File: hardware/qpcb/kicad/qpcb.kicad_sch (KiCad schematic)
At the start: 9 parts, among them J1 SWD Connector, J2 UART0 Connector, U1 Pico

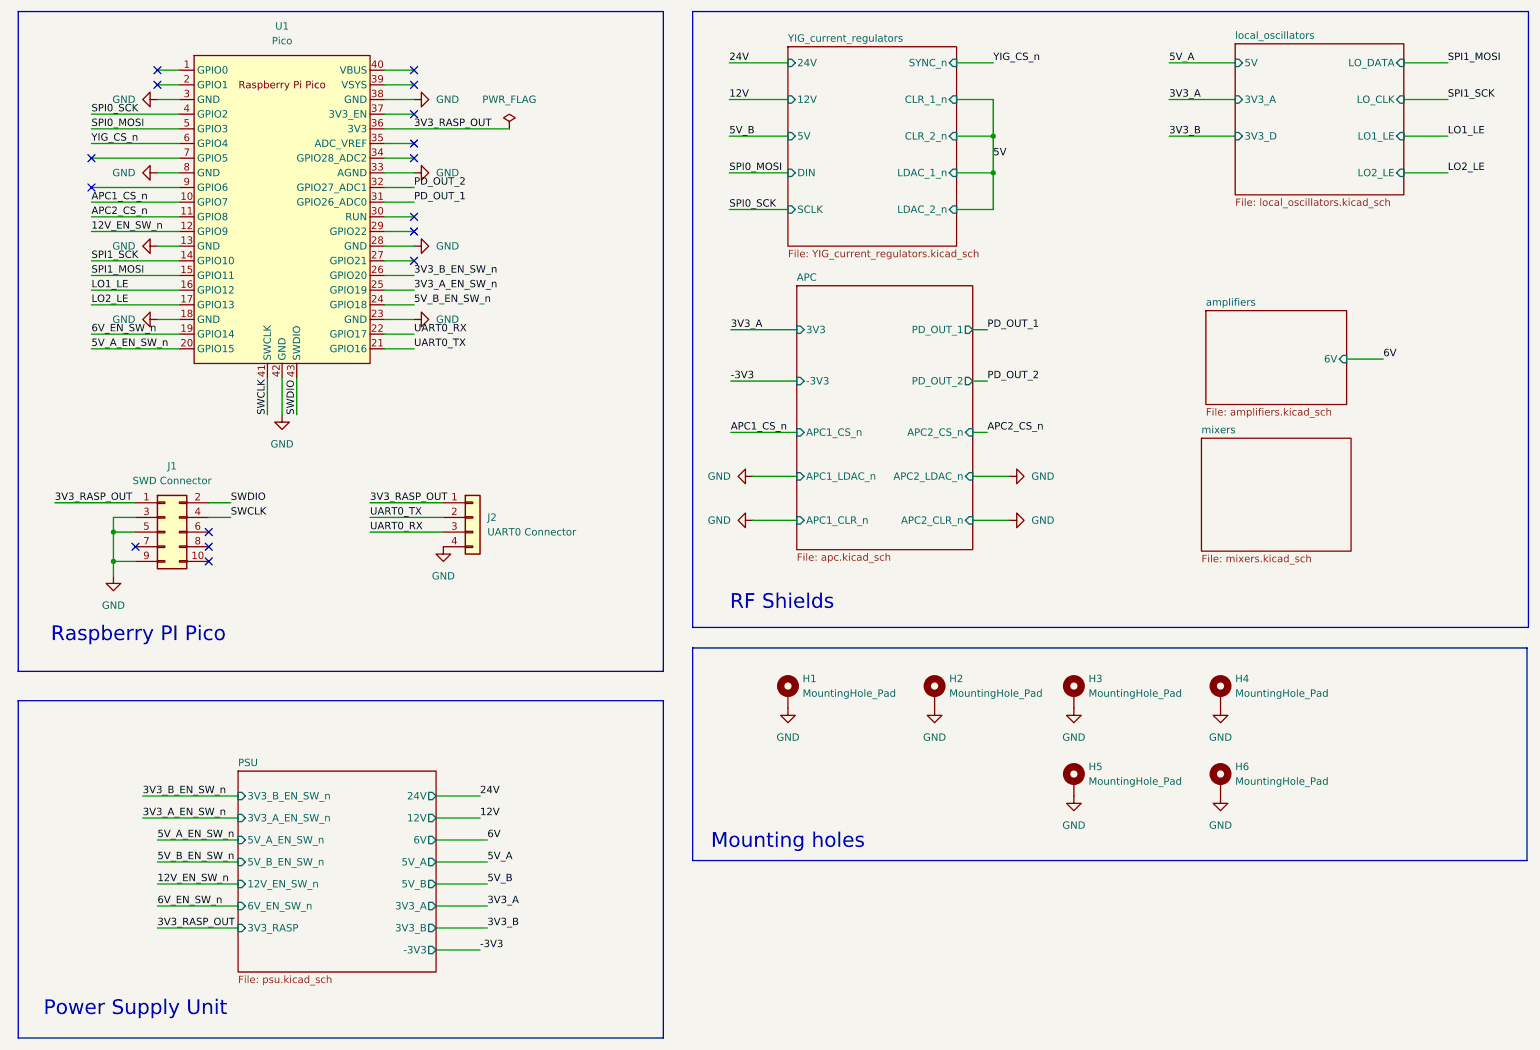
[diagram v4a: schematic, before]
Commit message: Add final footprints of daughter boards, change components for -3v3 power supply line and placement almost finished
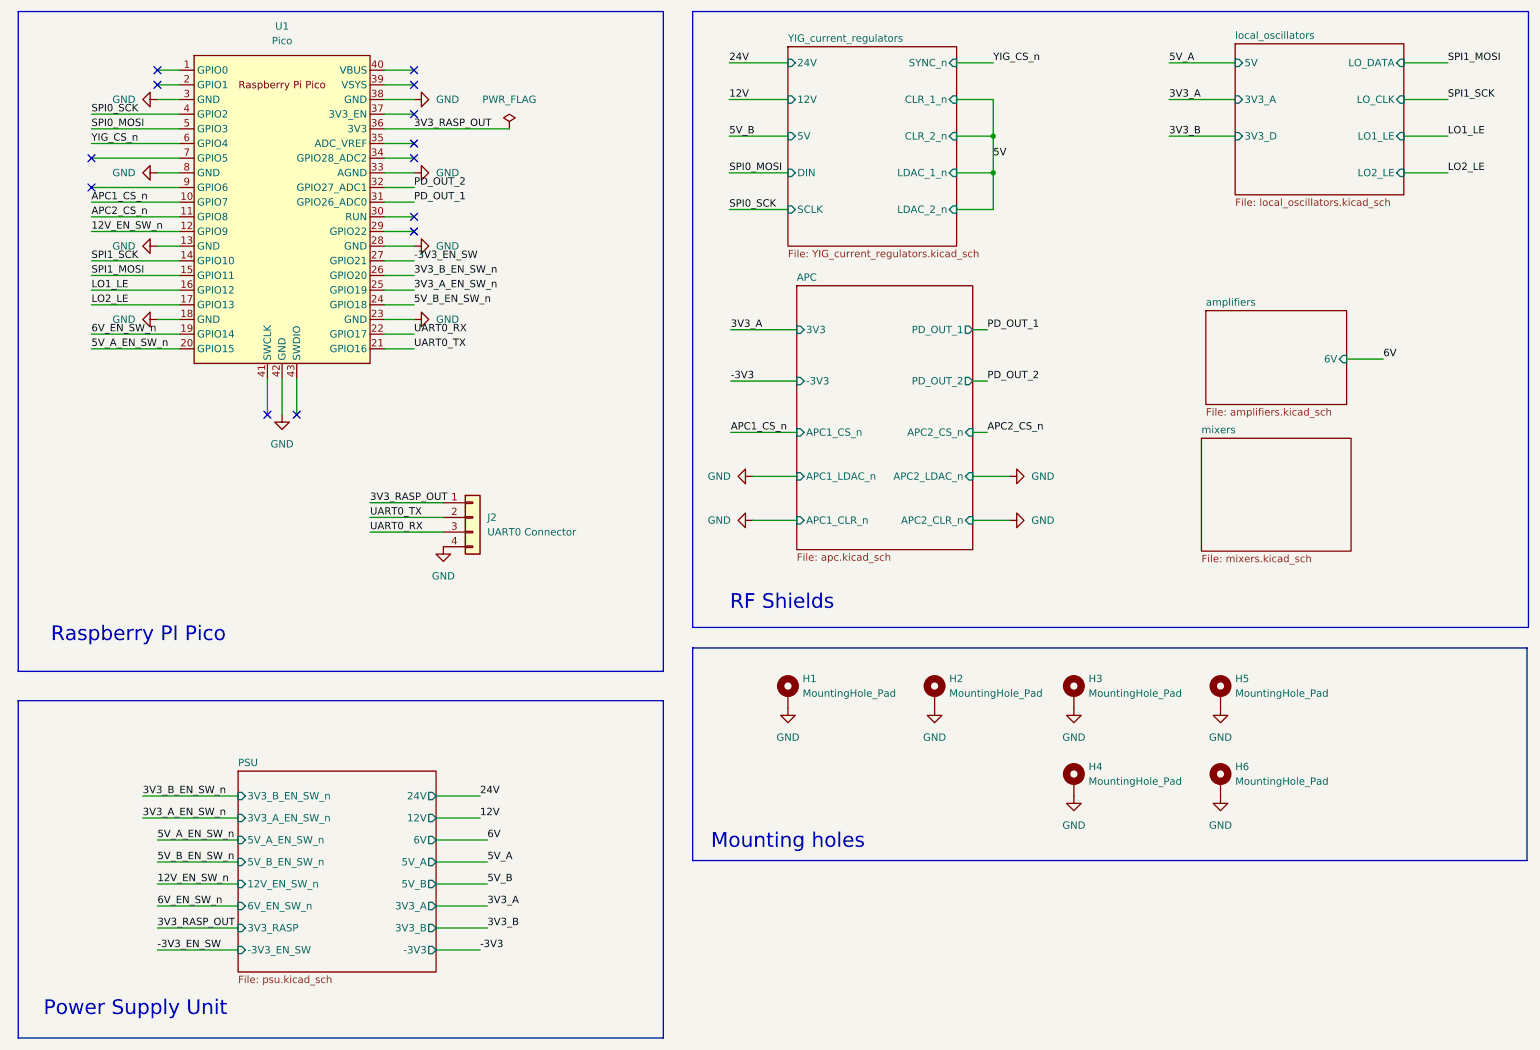
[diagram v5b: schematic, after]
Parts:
- removed J1: SWD Connector, symbol Connector_Generic:Conn_02x05_Odd_Even
- H1, H2, H3, H6: footprint (none) -> MountingHole:MountingHole_3.2mm_M3_DIN965_Pad
- H4: renamed from H5; footprint (none) -> MountingHole:MountingHole_3.2mm_M3_DIN965_Pad
- H5: renamed from H4; footprint (none) -> MountingHole:MountingHole_3.2mm_M3_DIN965_Pad
- J2: footprint (none) -> Connector_PinHeader_2.54mm:PinHeader_1x04_P2.54mm_Vertical
- U1: footprint RPi_Pico:RPi_Pico_SMD_TH -> footprints:RPi_Pico_SMD_TH
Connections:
- net -3V3_EN_SW: now reaches U1.27 (GPIO21)
- net SWCLK: no longer names the net of U1.41 (SWCLK)
- net SWDIO: no longer names the net of U1.43 (SWDIO)
- no-connect marks 16 -> 13
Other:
- sheet PSU ports: added -3V3_EN_SW; removed none

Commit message: Add QPCB JLCPCB production files
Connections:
- net -3V3_EN_SW: no longer names the net of U1.27 (GPIO21)
- net 12V_EN_SW_n: no longer names the net of U1.12 (GPIO9)
- net 3V3_A_EN_SW_n: no longer names the net of U1.25 (GPIO19)
- net 3V3_B_EN_SW_n: no longer names the net of U1.26 (GPIO20)
- net 5V_A_EN_SW_n: no longer names the net of U1.20 (GPIO15)
- net 5V_B_EN_SW_n: no longer names the net of U1.24 (GPIO18)
- net 6V_EN_SW_n: no longer names the net of U1.19 (GPIO14)
- no-connect marks 13 -> 20
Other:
- sheet PSU ports: added none; removed -3V3_EN_SW, 12V_EN_SW_n, 3V3_A_EN_SW_n, 3V3_B_EN_SW_n, 3V3_RASP, 5V_A_EN_SW_n, 5V_B_EN_SW_n, 6V_EN_SW_n
